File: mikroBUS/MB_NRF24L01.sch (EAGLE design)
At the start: 2 parts

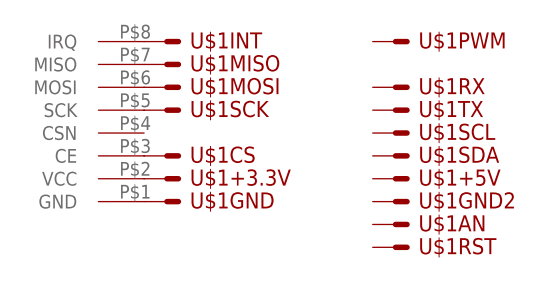
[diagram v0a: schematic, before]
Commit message: 
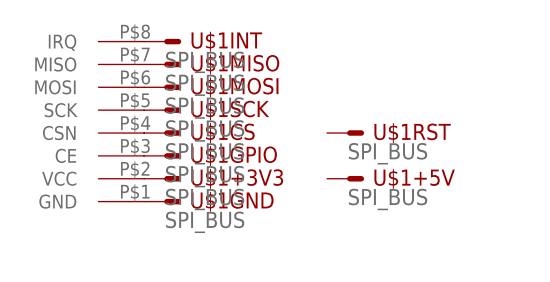
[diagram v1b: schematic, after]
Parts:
- U$1: value (none) -> SPI_BUS; device lieven:MIKROBUSSIL -> lieven:SPI_BUS
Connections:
- removed net N$3 (its old number): U$1CS.S, U$2.CE
- new net N$6: U$1CS.S, U$2.CSN
- new net N$8: U$1GPIO.S, U$2.CE
- net N$2: now also U$1+3V3.S; no longer U$1+3.3V.S
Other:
- moved on the sheet: U$1+5V, U$1CS, U$1RST
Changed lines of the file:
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@@
 </classes>
 <parts>
-<part name="U$1" library="lieven" deviceset="MIKROBUS" device="SIL"/>
 <part name="U$2" library="lieven" deviceset="RF24L01" device="MODULE"/>
+<part name="U$1" library="lieven" deviceset="SPI_BUS" device=""/>
 </parts>
 <sheets>
@@
 </plain>
 <instances>
-<instance part="U$1" gate="PWM" x="45.72" y="63.5"/>
+<instance part="U$2" gate="G$1" x="-7.62" y="60.96" rot="R180"/>
+<instance part="U$1" gate="GND" x="20.32" y="45.72"/>
+<instance part="U$1" gate="+3V3" x="20.32" y="48.26"/>
+<instance part="U$1" gate="+5V" x="40.64" y="48.26"/>
+<instance part="U$1" gate="MOSI" x="20.32" y="58.42"/>
+<instance part="U$1" gate="MISO" x="20.32" y="60.96"/>
+<instance part="U$1" gate="SCK" x="20.32" y="55.88"/>
+<instance part="U$1" gate="CS" x="20.32" y="53.34"/>
 <instance part="U$1" gate="INT" x="20.32" y="63.5"/>
-<instance part="U$1" gate="RX" x="45.72" y="58.42"/>
-<instance part="U$1" gate="TX" x="45.72" y="55.88"/>
-<instance part="U$1" gate="SCL" x="45.72" y="53.34"/>
-<instance part="U$1" gate="SDA" x="45.72" y="50.8"/>
-<instance part="U$1" gate="+5V" x="45.72" y="48.26"/>
-<instance part="U$1" gate="GND2" x="45.72" y="45.72"/>
-<instance part="U$1" gate="AN" x="45.72" y="43.18"/>
-<instance part="U$1" gate="RST" x="45.72" y="40.64"/>
-<instance part="U$1" gate="CS" x="20.32" y="50.8"/>
-<instance part="U$1" gate="SCK" x="20.32" y="55.88"/>
-<instance part="U$1" gate="MISO" x="20.32" y="60.96"/>
-<instance part="U$1" gate="MOSI" x="20.32" y="58.42"/>
-<instance part="U$1" gate="+3.3V" x="20.32" y="48.26"/>
-<instance part="U$1" gate="GND" x="20.32" y="45.72"/>
-<instance part="U$2" gate="G$1" x="-7.62" y="60.96" rot="R180"/>
+<instance part="U$1" gate="RST" x="40.64" y="53.34"/>
+<instance part="U$1" gate="GPIO" x="20.32" y="50.8"/>
 </instances>
 <busses>
@@
 <segment>
 <pinref part="U$2" gate="G$1" pin="VCC"/>
-<pinref part="U$1" gate="+3.3V" pin="S"/>
+<pinref part="U$1" gate="+3V3" pin="S"/>
 </segment>
 </net>
 <net name="N$3" class="0">
 <segment>
-<pinref part="U$2" gate="G$1" pin="CE"/>
-<pinref part="U$1" gate="CS" pin="S"/>
+<pinref part="U$2" gate="G$1" pin="MOSI"/>
+<pinref part="U$1" gate="MOSI" pin="S"/>
 </segment>
 </net>
@@
 <net name="N$5" class="0">
 <segment>
-<pinref part="U$2" gate="G$1" pin="MOSI"/>
-<pinref part="U$1" gate="MOSI" pin="S"/>
+<pinref part="U$2" gate="G$1" pin="SCK"/>
+<pinref part="U$1" gate="SCK" pin="S"/>
 </segment>
 </net>
 <net name="N$6" class="0">
 <segment>
-<pinref part="U$2" gate="G$1" pin="SCK"/>
-<pinref part="U$1" gate="SCK" pin="S"/>
+<pinref part="U$2" gate="G$1" pin="CSN"/>
+<pinref part="U$1" gate="CS" pin="S"/>
 </segment>
 </net>
@@
 </segment>
 </net>
+<net name="N$8" class="0">
+<segment>
+<pinref part="U$2" gate="G$1" pin="CE"/>
+<pinref part="U$1" gate="GPIO" pin="S"/>
+</segment>
+</net>
